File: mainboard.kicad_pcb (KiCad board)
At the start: 4 copper layers, 44.4 x 35.8 mm, 69 parts, among them J1 Conn_01x06, J2 USB_B_Micro, J3 xf2m-2415-1a, J4 XF2M-1015-1A, J5 Conn_01x02, J6 U.FL-R-SMT-1, Q1 RADFET, SW1 KMR231NG LFS, U1 BMX160, U10 TPS82740BSIPR, U2 MAX708RESA-T, U3 ATSAMD51J20A-M, U4 DRV8830DRC, U5 MR25H40, U6 DRV8830DRC, U7 ADS124S06IRHBR, U8 DRV8830DRC, U9 RFM98PW-symbols

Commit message: initial layout done
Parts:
- moved Q1 35.1 mm to (118.2, 87.9), turned to 270 degrees
- moved R22 29.8 mm to (118.2, 76.7), turned to 270 degrees
- moved R24 28.8 mm to (110.5, 78.5), turned to 270 degrees
- moved C15 28.6 mm to (113.8, 82.2), turned to 0 degrees
- moved C16 28.2 mm to (110.5, 76.5), turned to 90 degrees
- moved U7 27.9 mm to (114.5, 78.8)
- moved C14 27.7 mm to (110.5, 80.5)
- moved R6 4.28 mm to (90.0, 95.5)
- moved D1 3.36 mm to (87.3, 95.5)
- moved R21 0.75 mm to (116.0, 84.0)
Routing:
- net ADC_CS: track 0.00 -> 74.6 mm, vias 0 -> 2
- net MOSI: track 39.9 -> 53.9 mm, vias 3 -> 4
- net MISO: track 41.2 -> 55.0 mm, vias 3 -> 4
- net SCK: track 41.4 -> 55.0 mm, vias 3 -> 4
- net Net-(Q1-Pad4): track 6.03 -> 17.7 mm, vias 0 -> 2
- net +3V3: track 51.8 -> 59.1 mm, vias 15 -> 17
- net Net-(Q1-Pad2): track 4.26 -> 9.51 mm, vias 0 -> 2
- net Net-(R6-Pad1): track 1.34 -> 5.74 mm
- net Net-(R24-Pad2): track 0.00 -> 2.62 mm
- net Net-(C14-Pad1): track 0.00 -> 1.35 mm
- net Net-(D1-Pad2): track 2.28 -> 1.25 mm

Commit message: RGB LED
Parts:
- removed R6: 470R, Resistor_SMD:R_0402_1005Metric
- D1: value LED -> WS2812B; footprint LED_SMD:LED_0805_2012Metric -> LED_SMD:LED_WS2812B_PLCC4_5.0x5.0mm_P3.2mm
- moved U10 7.83 mm to (87.8, 98.3)
- moved D1 6.40 mm to (81.0, 94.8)
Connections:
- D1 pad 1: (no net) -> +3V3
- D1 pad 2: Net-(D1-Pad2) -> (no net)
- U3 pad 42: Net-(R6-Pad1) -> Net-(D1-Pad4)
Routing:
- net Net-(D1-Pad4): track 0.00 -> 12.7 mm
- net Net-(R6-Pad1): track 5.74 -> 0.00 mm
- net +3V3: track 59.1 -> 60.4 mm, vias 17 -> 18
- net Net-(D1-Pad2): track 1.25 -> 0.00 mm
- net Net-(D2-Pad1): track 7.37 -> 6.17 mm

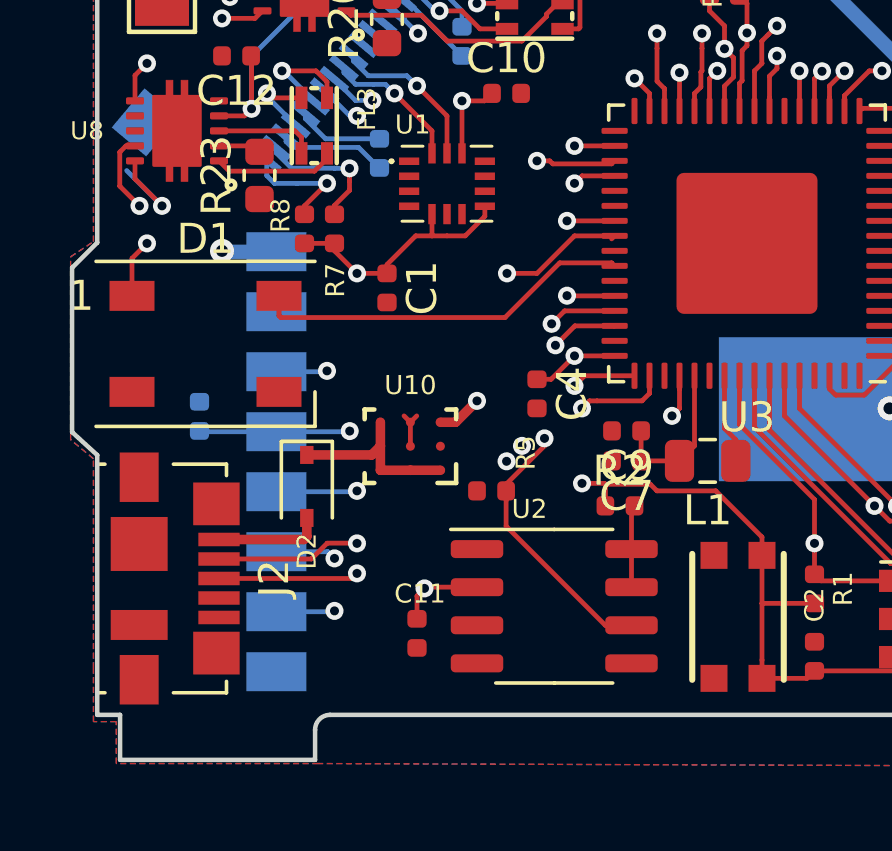
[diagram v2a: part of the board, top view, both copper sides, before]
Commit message: changed LDO and added RBF header
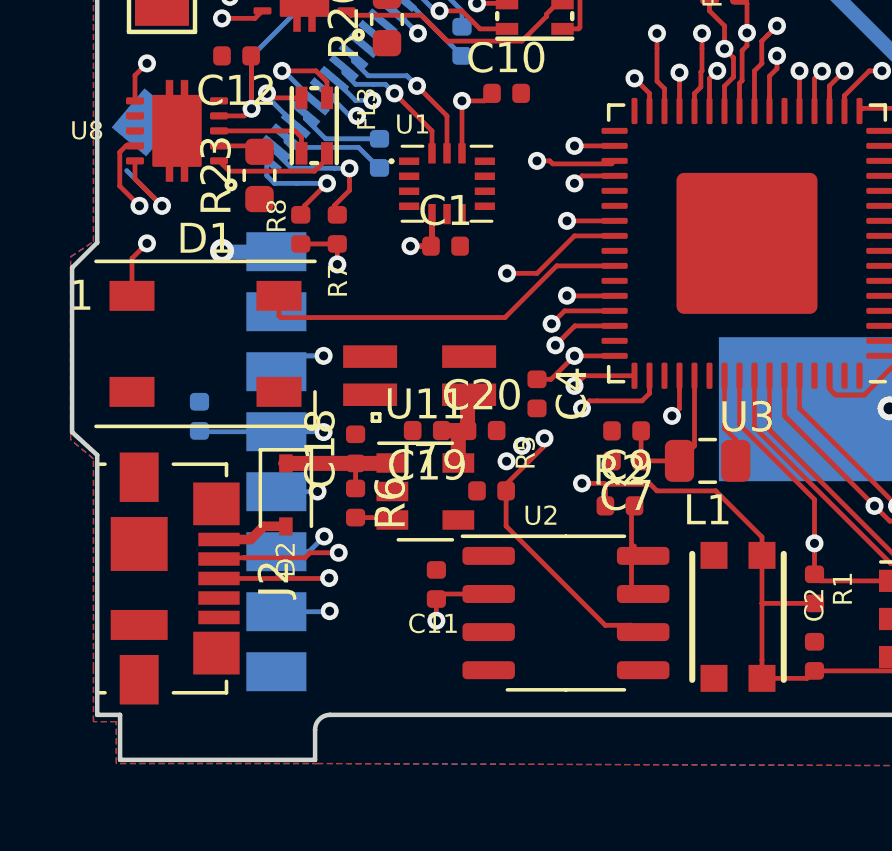
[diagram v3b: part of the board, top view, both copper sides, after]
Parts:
- removed U10: TPS82740BSIPR, custom-footprints:TPS82740ASIPR
- added C18: 10uF, Capacitor_SMD:C_0402_1005Metric, F.Cu at (86.0, 98.3)
- added C19: 10uF, Capacitor_SMD:C_0402_1005Metric, F.Cu at (88.3, 97.7)
- added C20: 1uF, Capacitor_SMD:C_0402_1005Metric, F.Cu at (90.2, 97.7)
- added J7: Conn_02x02_Top_Bottom, Connector_PinSocket_1.27mm:PinSocket_2x02_P1.27mm_Vertical_SMD, F.Cu at (88.1, 95.9)
- added R6: 10K, Resistor_SMD:R_0402_1005Metric, F.Cu at (86.0, 100.2)
- added U11: AP2112K-3.3, Package_TO_SOT_SMD:SOT-23-5, F.Cu at (88.3, 99.8)
- moved C1 2.40 mm to (89.0, 91.6), turned to 0 degrees
- moved C11 1.75 mm to (88.6, 102.9), turned to 90 degrees
- moved D2 0.75 mm to (83.6, 99.9)
- moved U2 0.45 mm to (93.0, 103.8)
- moved R8 0.13 mm to (84.1, 91.0)
- moved R7 0.10 mm to (85.3, 91.0)
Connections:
- D1 pad 2: (no net) -> Net-(D1-Pad2)
- J1 pad 6: (no net) -> Net-(J1-Pad6)
- J2 pad 4: (no net) -> Net-(J2-Pad4)
- J3 pad 11: (no net) -> Net-(J3-Pad11)
- J4 pad 10: (no net) -> Net-(J4-Pad10)
- J4 pad 3: (no net) -> Net-(J4-Pad3)
- Q1 pad 1: (no net) -> Net-(Q1-Pad1)
- Q1 pad 3: (no net) -> Net-(Q1-Pad3)
- Q1 pad 5: (no net) -> Net-(Q1-Pad5)
- U1 pad 1: (no net) -> Net-(U1-Pad1)
- U1 pad 10: (no net) -> Net-(U1-Pad10)
- U1 pad 11: (no net) -> Net-(U1-Pad11)
- U1 pad 4: (no net) -> Net-(U1-Pad4)
- U1 pad 9: (no net) -> Net-(U1-Pad9)
- U2 pad 1: (no net) -> Net-(U2-Pad1)
- U2 pad 5: (no net) -> Net-(U2-Pad5)
- U3 pad 1: (no net) -> Net-(U3-Pad1)
- U3 pad 10: (no net) -> Net-(U3-Pad10)
- U3 pad 11: (no net) -> Net-(U3-Pad11)
- U3 pad 16: (no net) -> Net-(U3-Pad16)
- U3 pad 2: (no net) -> Net-(U3-Pad2)
- U3 pad 3: (no net) -> Net-(U3-Pad3)
- U3 pad 32: (no net) -> Net-(U3-Pad32)
- U3 pad 37: (no net) -> Net-(U3-Pad37)
- U3 pad 38: (no net) -> Net-(U3-Pad38)
- U3 pad 4: (no net) -> Net-(U3-Pad4)
- U3 pad 41: (no net) -> Net-(U3-Pad41)
- U3 pad 43: (no net) -> Net-(U3-Pad43)
- U3 pad 5: (no net) -> Net-(U3-Pad5)
- U3 pad 51: (no net) -> Net-(U3-Pad51)
- U3 pad 6: (no net) -> Net-(U3-Pad6)
- U3 pad 61: (no net) -> M_EN
- U3 pad 63: (no net) -> Net-(U3-Pad63)
- U3 pad 64: (no net) -> Net-(U3-Pad64)
- U3 pad 9: (no net) -> Net-(U3-Pad9)
- U7 pad 13: (no net) -> ~DRDY
- U7 pad 19: (no net) -> Net-(U7-Pad19)
- U7 pad 2: (no net) -> Net-(U7-Pad2)
- U7 pad 20: (no net) -> Net-(U7-Pad20)
- U7 pad 21: (no net) -> Net-(U7-Pad21)
- U7 pad 22: (no net) -> Net-(U7-Pad22)
- U7 pad 25: (no net) -> Net-(U7-Pad25)
- U7 pad 29: (no net) -> Net-(U7-Pad29)
- U7 pad 3: (no net) -> Net-(U7-Pad3)
- U7 pad 30: (no net) -> Net-(U7-Pad30)
- U7 pad 31: (no net) -> Net-(U7-Pad31)
- U7 pad 32: (no net) -> Net-(U7-Pad32)
- U7 pad 4: (no net) -> Net-(U7-Pad4)
- U7 pad 5: (no net) -> Net-(U7-Pad5)
- U9 pad 15: (no net) -> Net-(U9-Pad15)
- U9 pad 3: (no net) -> Net-(U9-Pad3)
- U9 pad 6: (no net) -> Net-(U9-Pad6)
- U9 pad 8: (no net) -> RF_IO2
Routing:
- net +3V3: track 60.4 -> 53.7 mm
- net ADC_CS: track 74.6 -> 77.9 mm
- net Net-(C19-Pad1): track 0.00 -> 3.16 mm
- net Net-(C18-Pad1): track 6.17 -> 4.37 mm
- net GND: track 8.26 -> 6.86 mm
- net Net-(R6-Pad2): track 0.00 -> 1.26 mm
- net VUSB: track 3.59 -> 2.41 mm
- net MISO: track 55.0 -> 55.9 mm

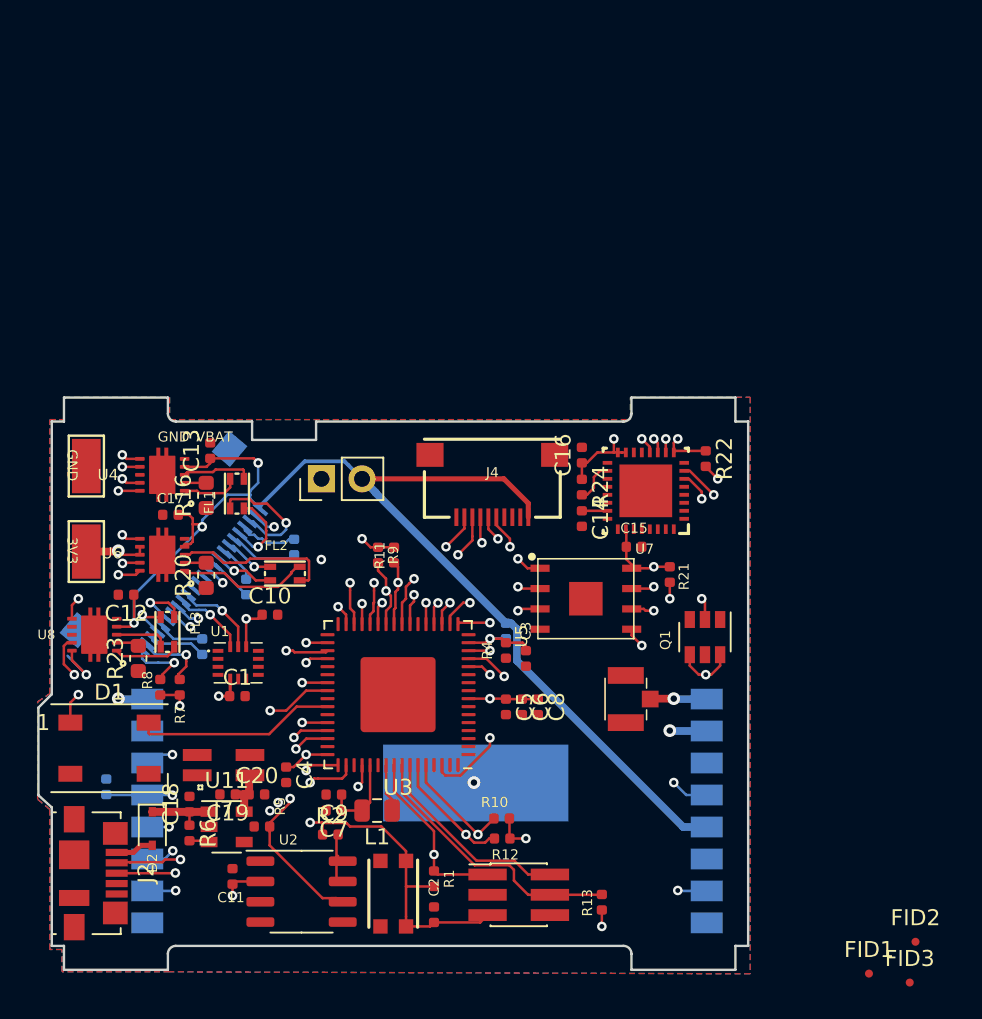
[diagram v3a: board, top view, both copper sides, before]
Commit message: BATT_P cleanup. starting dosimeter tweaks
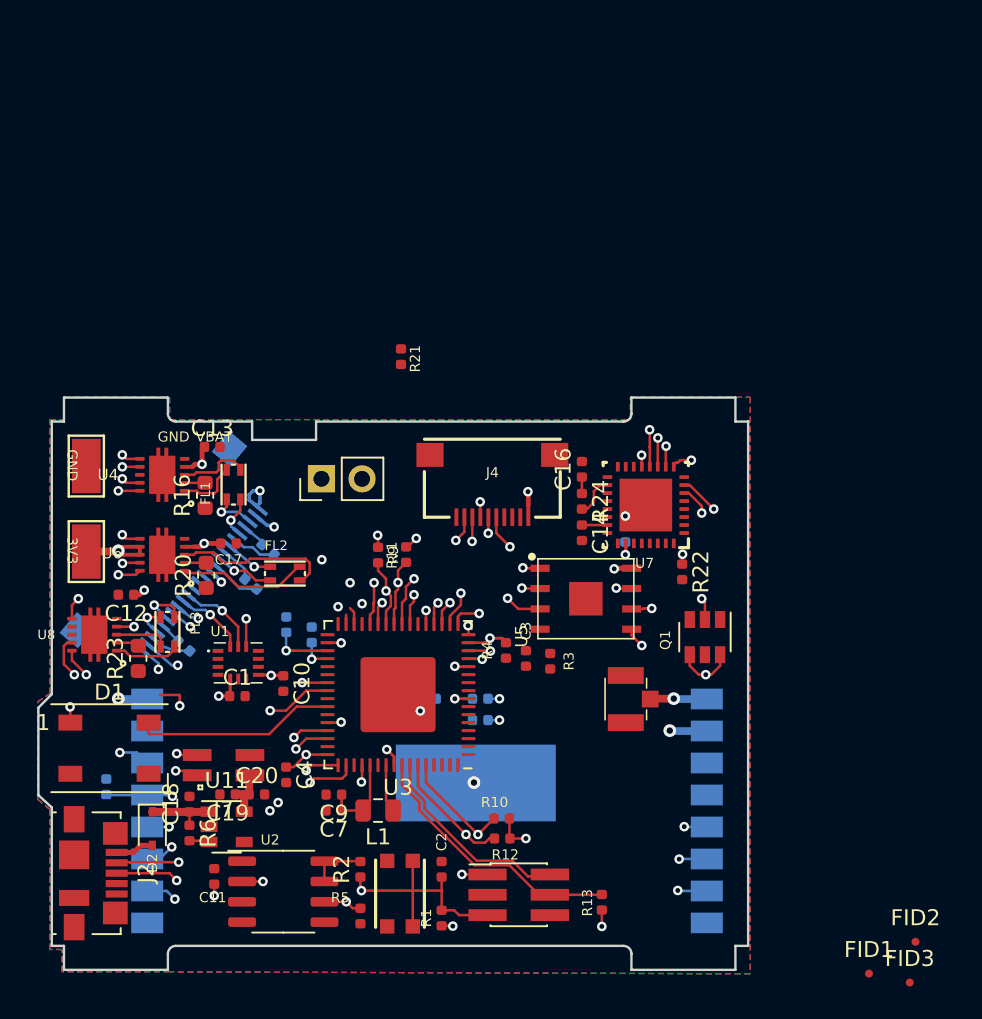
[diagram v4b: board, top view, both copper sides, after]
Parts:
- C15, C5, C6, C8, R7, R8: moved to B.Cu
- R3: moved to F.Cu
- moved R21 21.6 mm to (99.2, 70.4)
- moved R7 8.88 mm to (93.6, 87.8), turned to 90 degrees
- moved R8 8.80 mm to (92.0, 87.1), turned to 90 degrees
- moved R5 8.32 mm to (96.6, 105.3), turned to 90 degrees
- moved R22 7.24 mm to (116.8, 83.8)
- moved C6 5.87 mm to (100.9, 91.8), turned to 180 degrees
- moved C10 4.39 mm to (91.8, 90.8), turned to 270 degrees
- moved C17 4.05 mm to (88.4, 82.0), turned to 0 degrees
- moved C8 3.70 mm to (104.1, 93.1), turned to 0 degrees
- moved R3 3.36 mm to (108.5, 89.4), turned to 270 degrees
- moved C2 2.88 mm to (101.7, 102.4)
- moved R2 2.88 mm to (96.6, 102.4), turned to 90 degrees
- moved R1 2.50 mm to (101.7, 105.5), turned to 270 degrees
- moved C5 1.69 mm to (104.1, 91.8), turned to 0 degrees
- moved R19 1.64 mm to (90.9, 82.4), turned to 140 degrees
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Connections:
- U3 pad 14: RF_BUSY -> RF_IO0
- U3 pad 16: Net-(U3-Pad16) -> ADC_DRDY
- U7 pad 13: ~DRDY -> ADC_DRDY
- U9 pad 4: RF_BUSY -> Net-(U9-Pad4)
- U9 pad 6: Net-(U9-Pad6) -> RF_IO0
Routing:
- net M_FAULT: track 75.6 -> 39.9 mm, vias 5 -> 3
- net RF_IO0: track 0.00 -> 23.6 mm, vias 0 -> 2
- net ADC_DRDY: track 0.00 -> 22.0 mm, vias 0 -> 2
- net +3V3: track 53.7 -> 34.8 mm, vias 18 -> 23
- net RF_BUSY: track 18.6 -> 0.00 mm, vias 2 -> 0
- net BATT_P: track 79.2 -> 61.8 mm, vias 3 -> 8
- net Net-(Q1-Pad4): track 17.7 -> 6.92 mm
- net ADC_CS: track 77.9 -> 69.2 mm, vias 2 -> 3
- net Net-(Q1-Pad2): track 9.51 -> 3.26 mm
- net COIL1_P: track 7.84 -> 2.94 mm
- net RF_RST: track 22.6 -> 26.7 mm
- net SDA3: track 56.4 -> 59.9 mm
- net RF_CS: track 29.4 -> 26.1 mm
- net FLASH_IO3: track 17.2 -> 14.4 mm
- net GND: track 6.86 -> 9.52 mm, vias 5 -> 9
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
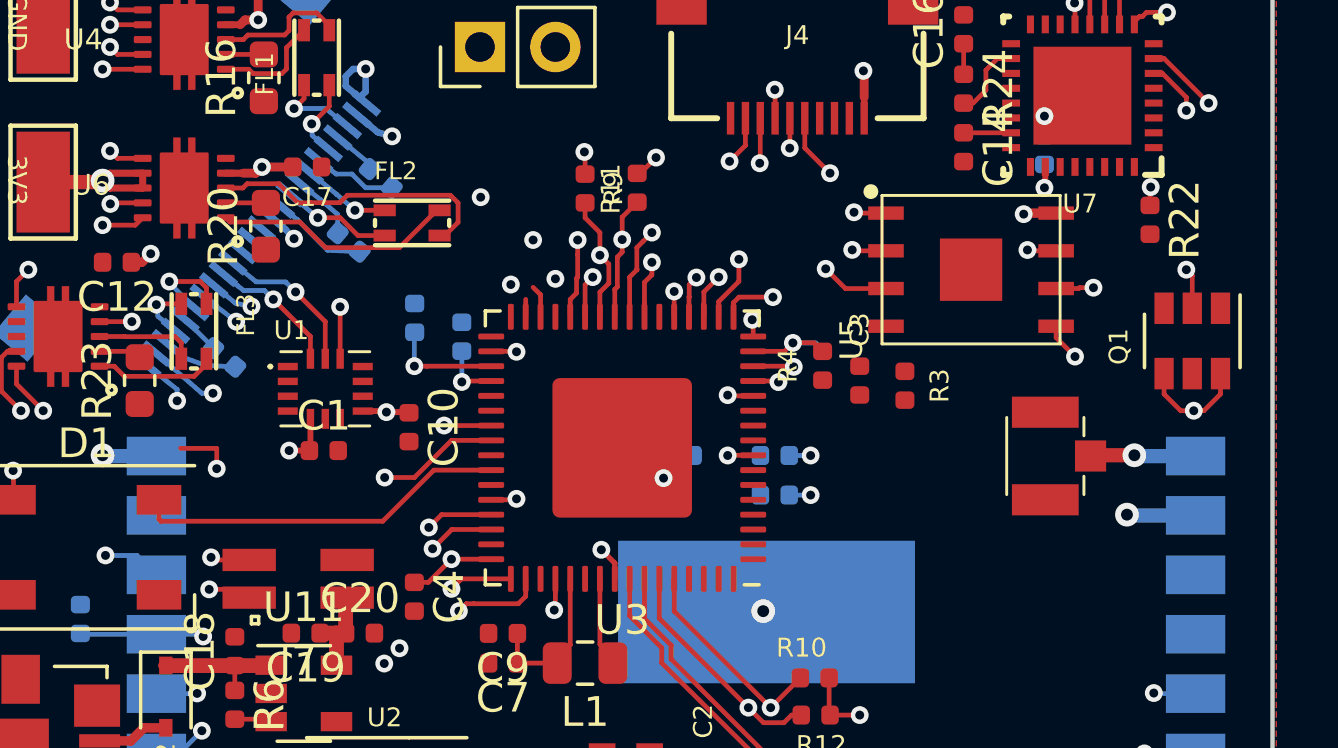
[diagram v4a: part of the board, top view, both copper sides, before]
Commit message: fit-checked with CAD
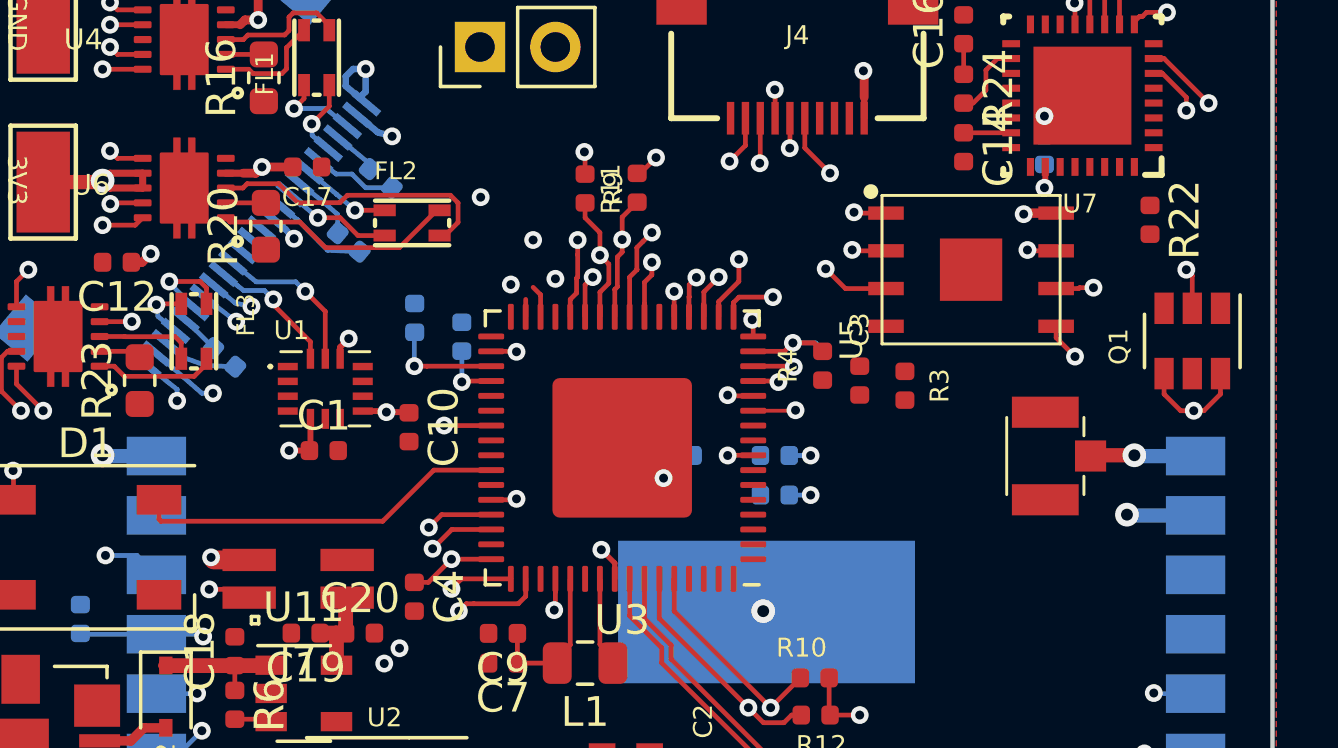
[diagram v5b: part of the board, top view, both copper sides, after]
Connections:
- U3 pad 11: Net-(U3-Pad11) -> ADC_CS
- U3 pad 40: ADC_CS -> Net-(U3-Pad40)
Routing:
- net ADC_CS: track 69.2 -> 2.75 mm, vias 3 -> 2
- net +3V3: track 34.8 -> 31.9 mm, vias 23 -> 22
